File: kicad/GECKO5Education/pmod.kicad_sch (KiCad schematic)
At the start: 32 parts, among them J4 Conn_02x09_Odd_Even, SW6 B3U-1000P[], U13 NCP1529A, U14 NCP1529A, U18 DS1338Z-33+T&R, U6 LFE5U-85F-6BG381x, U8 LP5907MFX-2.5, X2 ECS-2520MV-500-BL-TR, X3 CB3LV-3I-74M2500, X4 ECS-2520MV-240-BL-TR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

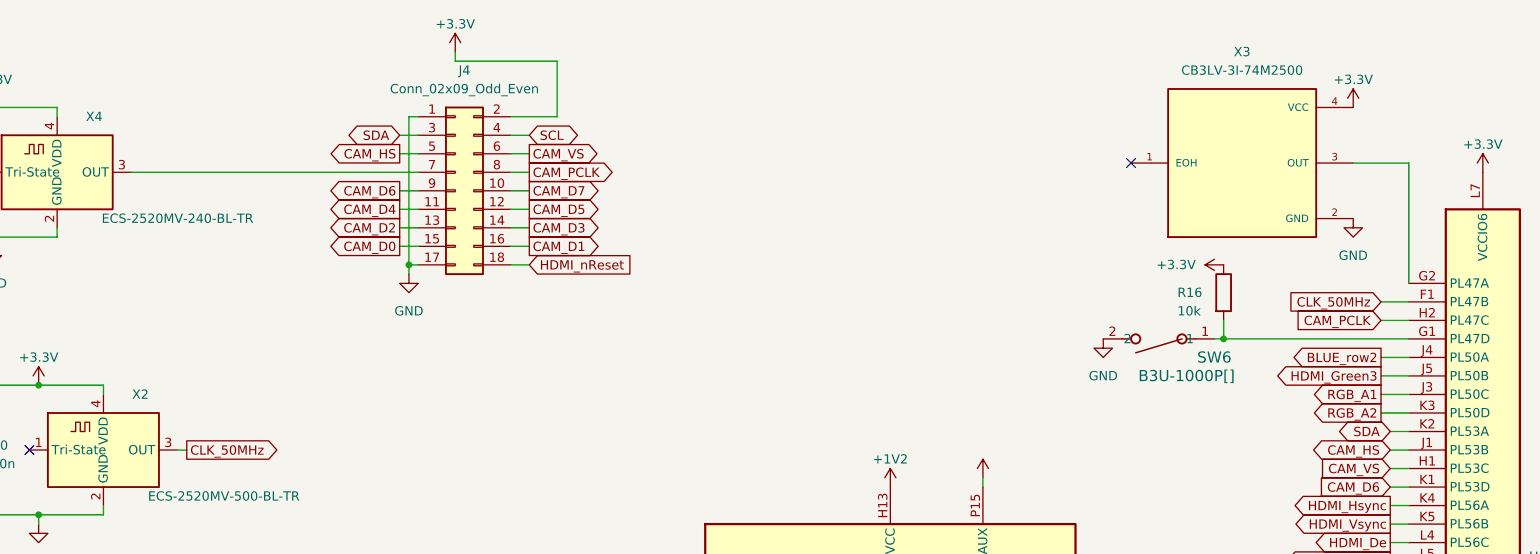
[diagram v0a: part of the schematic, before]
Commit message: Merged perif-add-on to GECKO5
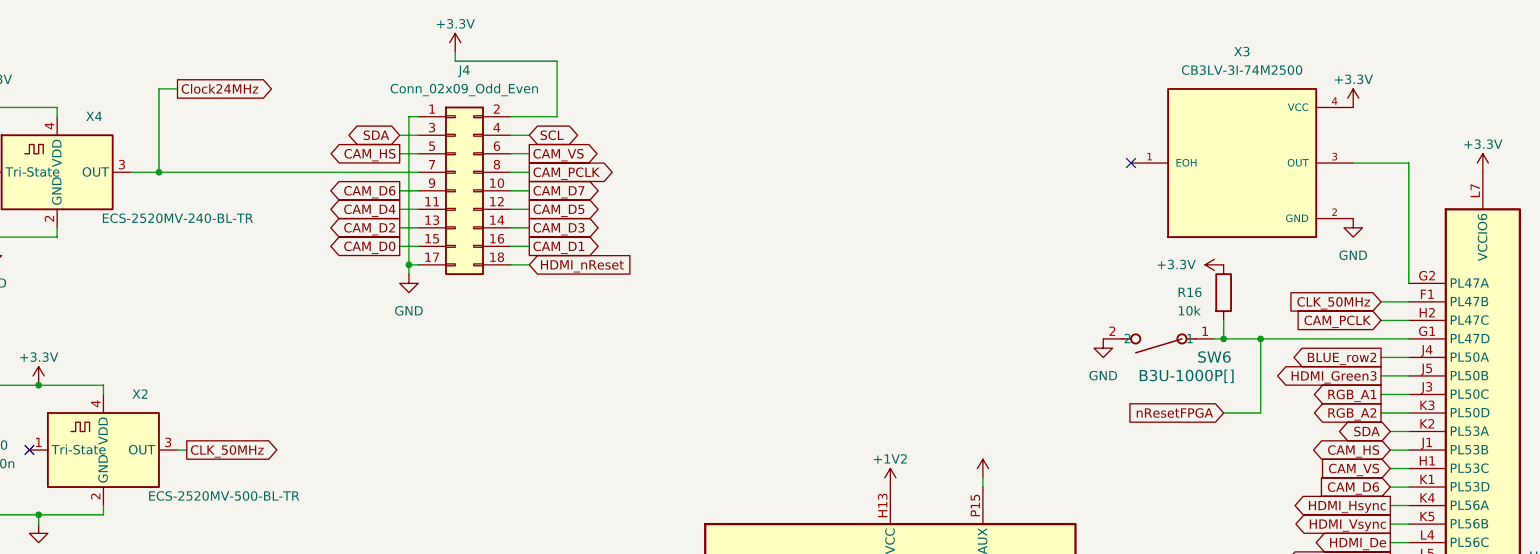
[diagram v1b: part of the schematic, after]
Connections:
- net nResetFPGA: now reaches R16.2, SW6.1, U6.G1 (PL47D)
- net Clock24MHz: now reaches J4.7 (Pin_7), X4.3 (OUT)
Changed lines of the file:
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@@
   (junction (at 49.53 44.45) (diameter 0) (color 0 0 0 0)
   )
+  (junction (at 223.52 58.42) (diameter 0) (color 0 0 0 0)
+  )
   (junction (at 109.22 138.43) (diameter 0) (color 0 0 0 0)
   )
@@
   )
   (junction (at 96.52 104.14) (diameter 0) (color 0 0 0 0)
+  )
+  (junction (at 72.39 35.56) (diameter 0) (color 0 0 0 0)
   )
   (junction (at 58.42 189.23) (diameter 0) (color 0 0 0 0)
@@
     (stroke (width 0) (type default))
   )
+  (wire (pts (xy 72.39 24.13) (xy 72.39 35.56))
+    (stroke (width 0) (type default))
+  )
+  (wire (pts (xy 74.93 24.13) (xy 72.39 24.13))
+    (stroke (width 0) (type default))
+  )
   (wire (pts (xy 64.77 114.3) (xy 64.77 119.38))
     (stroke (width 0) (type default))
@@
     (stroke (width 0) (type default))
   )
+  (wire (pts (xy 72.39 35.56) (xy 107.95 35.56))
+    (stroke (width 0) (type default))
+  )
   (wire (pts (xy 80.01 189.23) (xy 80.01 182.88))
     (stroke (width 0) (type default))
@@
     (stroke (width 0) (type default))
   )
+  (wire (pts (xy 223.52 68.58) (xy 223.52 58.42))
+    (stroke (width 0) (type default))
+  )
   (wire (pts (xy 48.26 104.14) (xy 57.15 104.14))
     (stroke (width 0) (type default))
@@
     (stroke (width 0) (type default))
   )
+  (wire (pts (xy 218.44 68.58) (xy 223.52 68.58))
+    (stroke (width 0) (type default))
+  )
   (wire (pts (xy 48.26 101.6) (xy 48.26 104.14))
     (stroke (width 0) (type default))
@@
     (stroke (width 0) (type default))
   )
-  (wire (pts (xy 218.44 58.42) (xy 243.84 58.42))
+  (wire (pts (xy 218.44 58.42) (xy 223.52 58.42))
     (stroke (width 0) (type default))
   )
@@
     (stroke (width 0) (type default))
   )
+  (wire (pts (xy 223.52 58.42) (xy 243.84 58.42))
+    (stroke (width 0) (type default))
+  )
   (wire (pts (xy 58.42 189.23) (xy 62.23 189.23))
     (stroke (width 0) (type default))
@@
     (stroke (width 0) (type default))
   )
-  (wire (pts (xy 68.58 35.56) (xy 107.95 35.56))
+  (wire (pts (xy 68.58 35.56) (xy 72.39 35.56))
     (stroke (width 0) (type default))
   )
@@
     )
   )
+  (global_label "Clock24MHz" (shape output) (at 74.93 24.13 0) (fields_autoplaced)
+    (effects (font (size 1.27 1.27)) (justify left))
+    (property "Intersheetrefs" "${INTERSHEET_REFS}" (at 89.3451 24.13 0)
+      (effects (font (size 1.27 1.27)) (justify left) hide)
+    )
+  )
   (global_label "CAM_D6" (shape input) (at 241.3 78.74 180) (fields_autoplaced)
     (effects (font (size 1.27 1.27)) (justify right))
@@
       (effects (font (size 1.27 1.27)) (justify right) hide)
     )
+  )
+  (global_label "nResetFPGA" (shape input) (at 218.44 68.58 180) (fields_autoplaced)
+    (effects (font (size 1.27 1.27)) (justify right))
+    (property "Intersheetrefs" "${INTERSHEET_REFS}" (at 204.3876 68.58 0)
+      (effects (font (size 1.27 1.27)) (justify right) hide)
+    )
